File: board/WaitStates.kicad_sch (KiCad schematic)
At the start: 6 parts, among them U84 ATF22V10C-10PU, U87 ATF16V8C-10PU

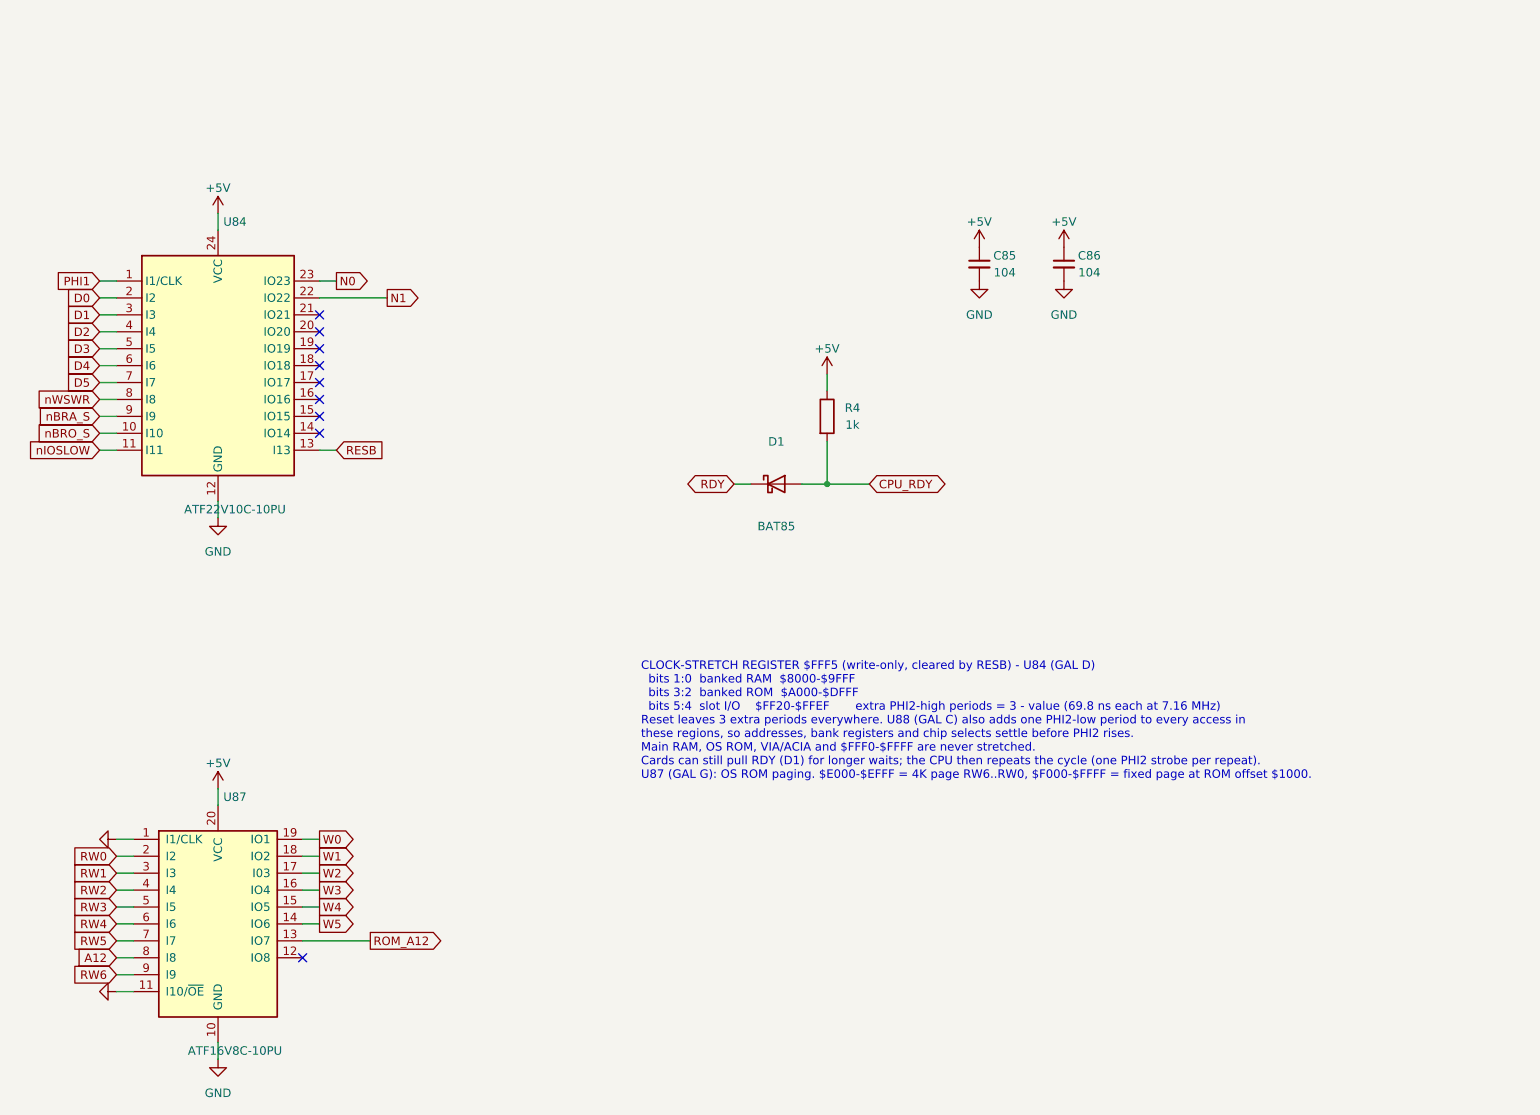
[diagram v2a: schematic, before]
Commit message: V2.0: speaker headers, A/D bus fix, layout edits
- On-board speakers LS1/LS2 replaced by 2-pin headers J40 (SPEAKER L)
  and J41 (SPEAKER R) for external mini speakers: pin 1 speaker
  (through R30/R31), pin 2 GNDA; J18 still mutes them
- Connectors: a layout move had joined the A[0..15] and D[0..7] buses
  at two crossings (shorting A0-A7 to D0-D7); buses separated again,
  connectivity matches the previous commit
- Layout edits across the sheets (no other connectivity change)
- PCB updated from the schematic

Co-Authored-By: Claude Opus 5.5 <noreply@anthropic.com>
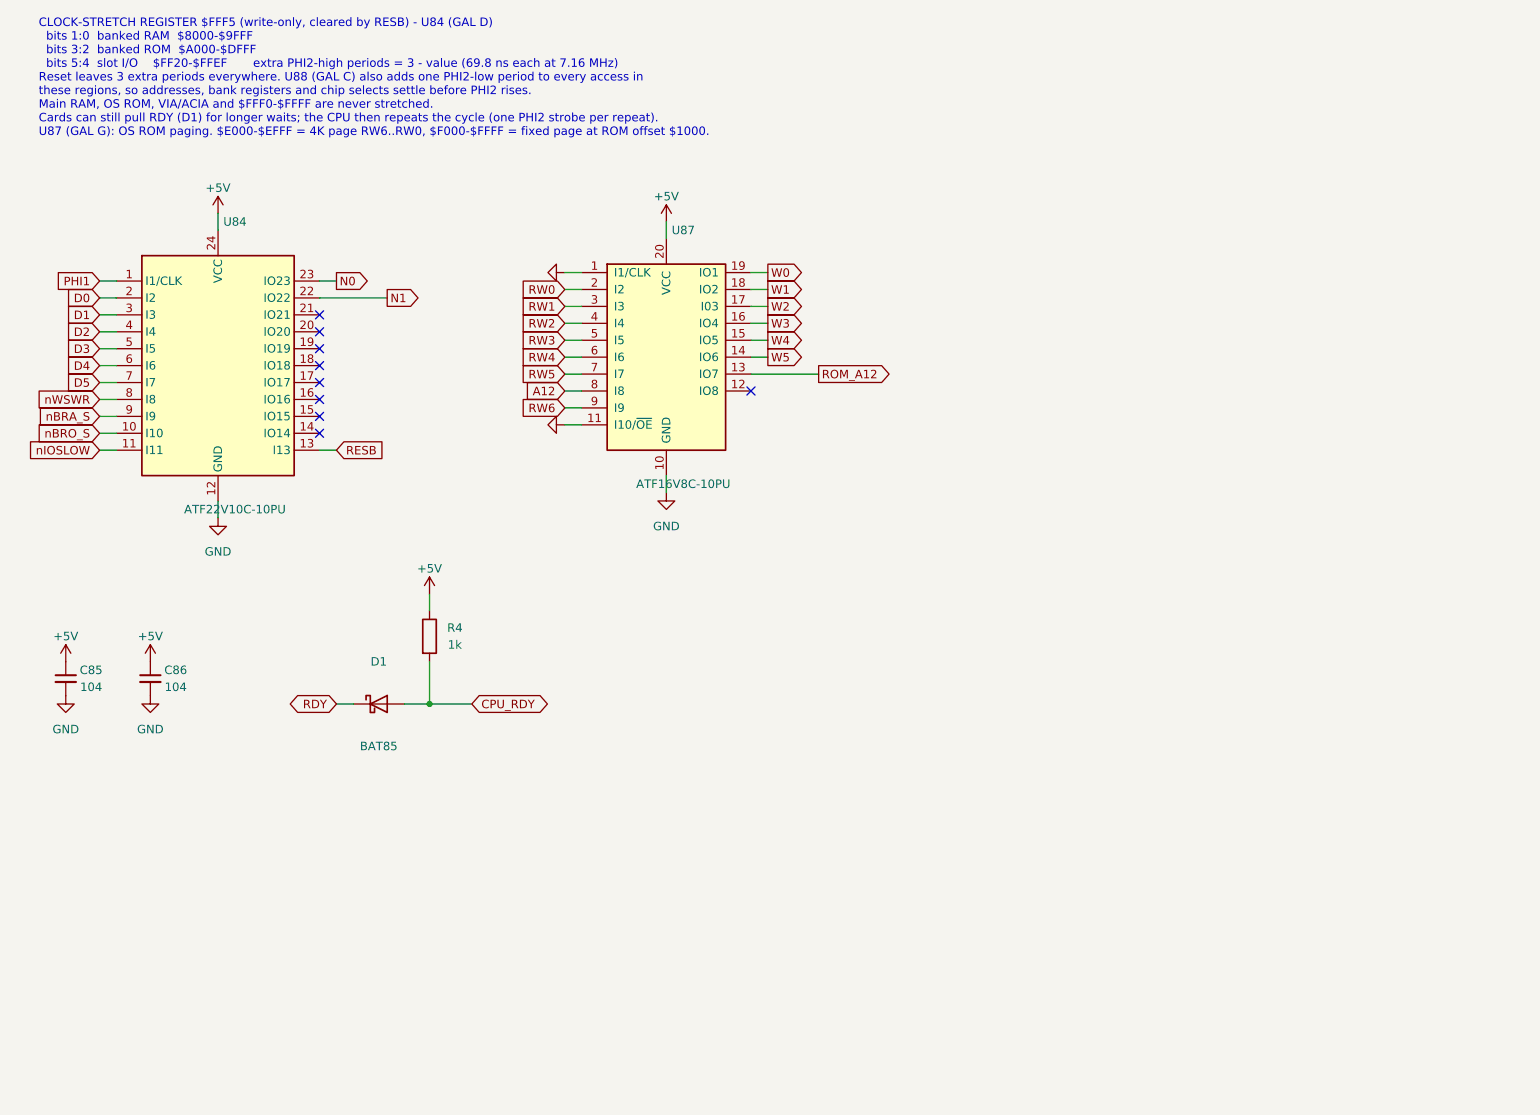
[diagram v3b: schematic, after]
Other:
- title: Clock-Stretch Control and OS ROM Paging (GALs) -> Expansion Slots, SPI Headers and Port A
- moved on the sheet: C85, C86, D1, R4, U87
